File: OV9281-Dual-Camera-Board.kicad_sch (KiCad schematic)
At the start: 82 parts, among them J3 Conn_FFC_WE_68715014522_TWO-S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, Q1 BSS138AKA, U1 ImageSensor_OV9281, U2 ImageSensor_OV9281, U3 NTS0104BQ, U4 NTB0104BQ, U5 TLV73318PDBVT, U6 TLV73312PDBVT, U7 TLV73328PDBVT, Y1 7C-24.000MBB-T, Y2 7C-24.000MBB-T

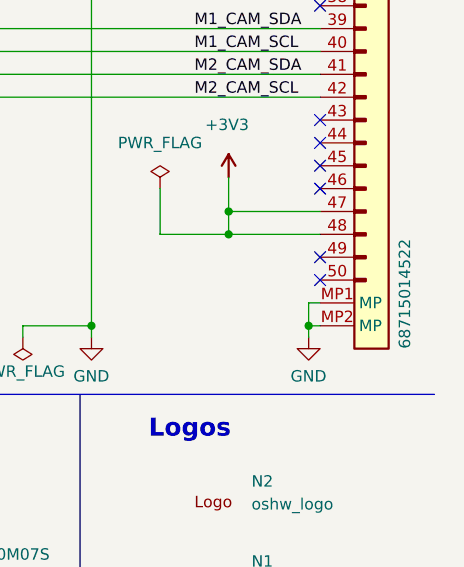
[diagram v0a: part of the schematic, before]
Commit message: Update FFC connector and standoffs
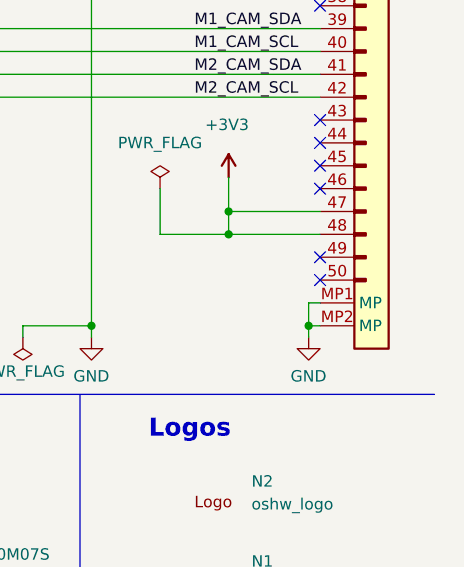
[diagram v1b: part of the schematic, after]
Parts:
- J3: symbol antmicroFCCConnectors:Conn_FFC_WE_68715014522_TWO-SIDES -> antmicroFCCConnectors:Conn_FFC_WE_68715014522_CUSTOM_TWO-SIDES; VSD_Class (none) -> Antmicro Dual Camera interface
- MP1, MP2, MP3, MP4: footprint antmicro-footprints:Spacer_SMD_M2_H3mm_Wurth_9774030243R -> antmicro-footprints:Spacer_Drill3mm_H3mm_9774030243R; symbol antmicroMechanicalParts:Spacer_H3mm_9774030243R -> antmicroMechanicalParts:Spacer_Drill3mm_H3mm_9774030243R
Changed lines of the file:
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@@
     (pin "1")
   )
-  (symbol (lib_id "antmicroFCCConnectors:Conn_FFC_WE_68715014522_TWO-SIDES") (at 394.97 26.67 0) (unit 1)
+  (symbol (lib_id "antmicroFCCConnectors:Conn_FFC_WE_68715014522_CUSTOM_TWO-SIDES") (at 394.97 26.67 0) (unit 1)
     (in_bom yes) (on_board yes)
     (property "Reference" "J3" (id 0) (at 403.86 90.8049 0)
@@
       (effects (font (size 1.27 1.27) (thickness 0.15)) (justify left bottom) hide)
     )
-    (property "MPN" "68715014522" (id 4) (at 405.13 158.75 90)
-      (effects (font (size 1.27 1.27) (thickness 0.15)) (justify left bottom))
+    (property "MPN" "68715014522" (id 4) (at 414.02 39.37 0)
+      (effects (font (size 1.27 1.27) (thickness 0.15)) (justify left bottom) hide)
     )
     (property "Manufacturer" "Würth Elektronik" (id 5) (at 414.02 41.91 0)
@@
       (effects (font (size 1.27 1.27) (thickness 0.15)) (justify left bottom) hide)
     )
+    (property "VSD_Class" "Antmicro Dual Camera interface" (id 8) (at 414.02 49.53 0)
+      (effects (font (size 1.27 1.27)) (justify left bottom) hide)
+    )
     (pin "1")
     (pin "10")
@@
     (pin "2")
   )
-  (symbol (lib_id "antmicroMechanicalParts:Spacer_H3mm_9774030243R") (at 369.57 229.87 0) (unit 1)
+  (symbol (lib_id "antmicroMechanicalParts:Spacer_Drill3mm_H3mm_9774030243R") (at 369.57 229.87 0) (unit 1)
     (in_bom yes) (on_board yes) (fields_autoplaced)
     (property "Reference" "MP3" (id 0) (at 378.46 228.5999 0)
@@
       (effects (font (size 1.27 1.27) (thickness 0.15)) (justify left))
     )
-    (property "Footprint" "antmicro-footprints:Spacer_SMD_M2_H3mm_Wurth_9774030243R" (id 2) (at 392.43 237.49 0)
+    (property "Footprint" "antmicro-footprints:Spacer_Drill3mm_H3mm_9774030243R" (id 2) (at 392.43 237.49 0)
       (effects (font (size 1.27 1.27) (thickness 0.15)) (justify left bottom) hide)
     )
-    (property "Datasheet" "https://katalog.we-online.de/em/datasheet/9774030243R.pdf" (id 3) (at 392.43 240.03 0)
+    (property "Datasheet" "https://www.we-online.com/components/products/datasheet/9774030243R.pdf" (id 3) (at 392.43 240.03 0)
       (effects (font (size 1.27 1.27) (thickness 0.15)) (justify left bottom) hide)
     )
@@
     (pin "1")
   )
-  (symbol (lib_id "antmicroMechanicalParts:Spacer_H3mm_9774030243R") (at 369.57 243.84 0) (unit 1)
+  (symbol (lib_id "antmicroMechanicalParts:Spacer_Drill3mm_H3mm_9774030243R") (at 369.57 243.84 0) (unit 1)
     (in_bom yes) (on_board yes) (fields_autoplaced)
     (property "Reference" "MP4" (id 0) (at 378.46 242.5699 0)
@@
       (effects (font (size 1.27 1.27) (thickness 0.15)) (justify left))
     )
-    (property "Footprint" "antmicro-footprints:Spacer_SMD_M2_H3mm_Wurth_9774030243R" (id 2) (at 392.43 251.46 0)
+    (property "Footprint" "antmicro-footprints:Spacer_Drill3mm_H3mm_9774030243R" (id 2) (at 392.43 251.46 0)
       (effects (font (size 1.27 1.27) (thickness 0.15)) (justify left bottom) hide)
     )
-    (property "Datasheet" "https://katalog.we-online.de/em/datasheet/9774030243R.pdf" (id 3) (at 392.43 254 0)
+    (property "Datasheet" "https://www.we-online.com/components/products/datasheet/9774030243R.pdf" (id 3) (at 392.43 254 0)
       (effects (font (size 1.27 1.27) (thickness 0.15)) (justify left bottom) hide)
     )
@@
     (pin "1")
   )
-  (symbol (lib_id "antmicroMechanicalParts:Spacer_H3mm_9774030243R") (at 369.57 215.9 0) (unit 1)
+  (symbol (lib_id "antmicroMechanicalParts:Spacer_Drill3mm_H3mm_9774030243R") (at 369.57 215.9 0) (unit 1)
     (in_bom yes) (on_board yes) (fields_autoplaced)
     (property "Reference" "MP2" (id 0) (at 378.46 214.6299 0)
@@
       (effects (font (size 1.27 1.27) (thickness 0.15)) (justify left))
     )
-    (property "Footprint" "antmicro-footprints:Spacer_SMD_M2_H3mm_Wurth_9774030243R" (id 2) (at 392.43 223.52 0)
+    (property "Footprint" "antmicro-footprints:Spacer_Drill3mm_H3mm_9774030243R" (id 2) (at 392.43 223.52 0)
       (effects (font (size 1.27 1.27) (thickness 0.15)) (justify left bottom) hide)
     )
-    (property "Datasheet" "https://katalog.we-online.de/em/datasheet/9774030243R.pdf" (id 3) (at 392.43 226.06 0)
+    (property "Datasheet" "https://www.we-online.com/components/products/datasheet/9774030243R.pdf" (id 3) (at 392.43 226.06 0)
       (effects (font (size 1.27 1.27) (thickness 0.15)) (justify left bottom) hide)
     )
@@
     (pin "2")
   )
-  (symbol (lib_id "antmicroMechanicalParts:Spacer_H3mm_9774030243R") (at 369.57 203.2 0) (unit 1)
+  (symbol (lib_id "antmicroMechanicalParts:Spacer_Drill3mm_H3mm_9774030243R") (at 369.57 203.2 0) (unit 1)
     (in_bom yes) (on_board yes) (fields_autoplaced)
     (property "Reference" "MP1" (id 0) (at 378.46 201.9299 0)
@@
       (effects (font (size 1.27 1.27) (thickness 0.15)) (justify left))
     )
-    (property "Footprint" "antmicro-footprints:Spacer_SMD_M2_H3mm_Wurth_9774030243R" (id 2) (at 392.43 210.82 0)
+    (property "Footprint" "antmicro-footprints:Spacer_Drill3mm_H3mm_9774030243R" (id 2) (at 392.43 210.82 0)
       (effects (font (size 1.27 1.27) (thickness 0.15)) (justify left bottom) hide)
     )
-    (property "Datasheet" "https://katalog.we-online.de/em/datasheet/9774030243R.pdf" (id 3) (at 392.43 213.36 0)
+    (property "Datasheet" "https://www.we-online.com/components/products/datasheet/9774030243R.pdf" (id 3) (at 392.43 213.36 0)
       (effects (font (size 1.27 1.27) (thickness 0.15)) (justify left bottom) hide)
     )
@@
     )
     (path "/00000000-0000-0000-0000-00005d948fb2"
-      (reference "MP1") (unit 1) (value "Spacer_H3mm_9774030243R") (footprint "antmicro-footprints:Spacer_SMD_M2_H3mm_Wurth_9774030243R")
+      (reference "MP1") (unit 1) (value "Spacer_H3mm_9774030243R") (footprint "antmicro-footprints:Spacer_Drill3mm_H3mm_9774030243R")
     )
     (path "/00000000-0000-0000-0000-00005d91c3cf"
-      (reference "MP2") (unit 1) (value "Spacer_H3mm_9774030243R") (footprint "antmicro-footprints:Spacer_SMD_M2_H3mm_Wurth_9774030243R")
+      (reference "MP2") (unit 1) (value "Spacer_H3mm_9774030243R") (footprint "antmicro-footprints:Spacer_Drill3mm_H3mm_9774030243R")
     )
     (path "/00000000-0000-0000-0000-00005d8efb53"
-      (reference "MP3") (unit 1) (value "Spacer_H3mm_9774030243R") (footprint "antmicro-footprints:Spacer_SMD_M2_H3mm_Wurth_9774030243R")
+      (reference "MP3") (unit 1) (value "Spacer_H3mm_9774030243R") (footprint "antmicro-footprints:Spacer_Drill3mm_H3mm_9774030243R")
     )
     (path "/00000000-0000-0000-0000-00005d8f000c"
-      (reference "MP4") (unit 1) (value "Spacer_H3mm_9774030243R") (footprint "antmicro-footprints:Spacer_SMD_M2_H3mm_Wurth_9774030243R")
+      (reference "MP4") (unit 1) (value "Spacer_H3mm_9774030243R") (footprint "antmicro-footprints:Spacer_Drill3mm_H3mm_9774030243R")
     )
     (path "/00000000-0000-0000-0000-00005e7b7776"

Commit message: Update components from library
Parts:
- U1, U2: footprint antmicro-footprints:ImageSensor_OV9281 -> antmicro-footprints:OV9281; symbol antmicroCameramodules:ImageSensor_OV9281 -> antmicroCameramodules:OV9281; Manufacturer ARDUCAM -> OmniVision
- Y1, Y2: footprint antmicro-footprints:7C-24.000MBB-T -> antmicro-footprints:Oscillator_SMD_TXC_7C_5x3.2x1.2mm; symbol antmicroOscillators:7C-24.000MBB-T -> antmicroOscillators:Oscillator_24MHz_TXC_7C; Val (none) -> 24 MHz

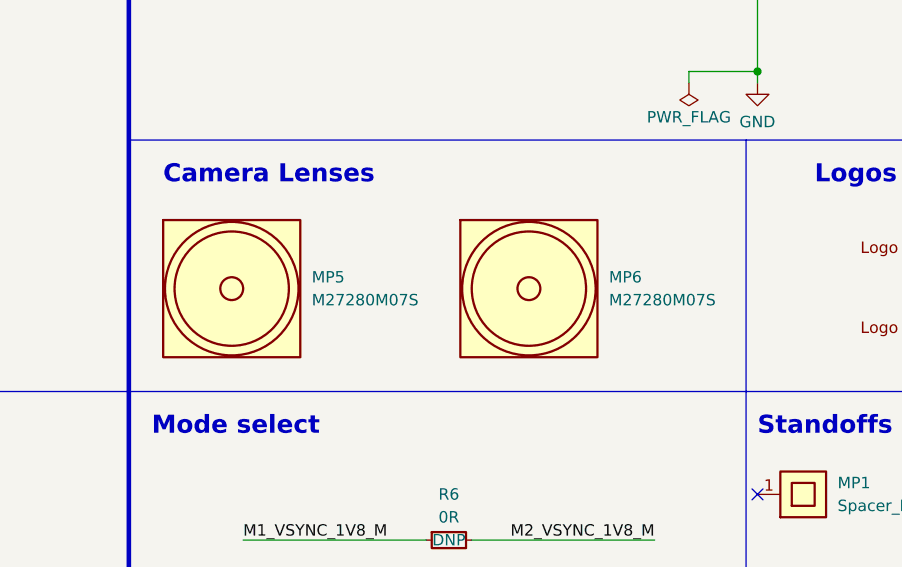
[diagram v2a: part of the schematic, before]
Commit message: Update components from libraries
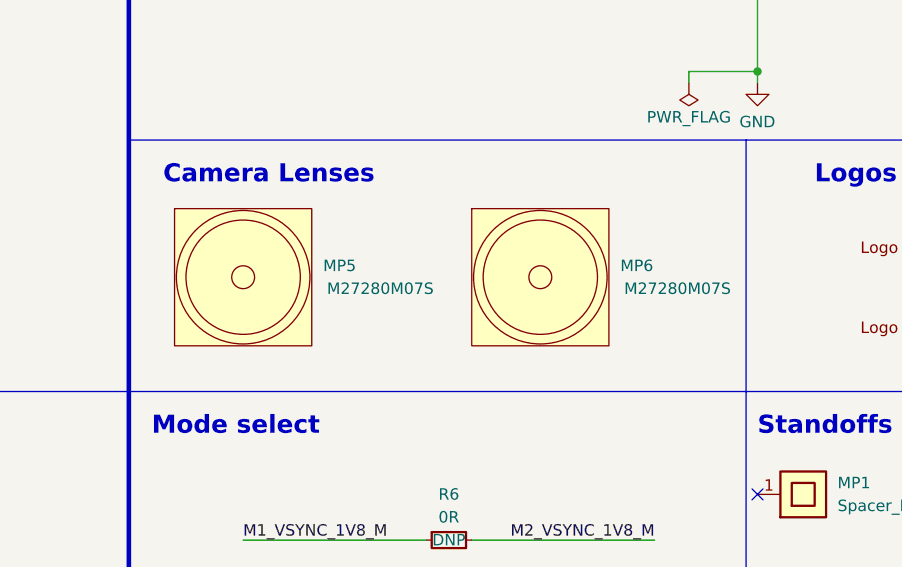
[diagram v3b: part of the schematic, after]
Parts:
- MP5, MP6: footprint antmicro-footprints:Camera_Lens_20mm_ARDUCAM_M27280M07S -> antmicro-footprints:Camera_Lens_20mm; now in the parts list
